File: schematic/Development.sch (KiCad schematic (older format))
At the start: 45 parts

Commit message: added partial summing difference amplifier
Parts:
- added C? (x2): C, symbol Device:C_Small
- added C? (x2): 100n, symbol Device:C_Small
- added J?: CONX, symbol Connector:Conn_Coaxial
- added J?: CONY, symbol Connector:Conn_Coaxial
- added R? (x12): R, symbol Device:R_Small
- added U? (x3): Opamp_Dual, symbol Device:Opamp_Dual_Generic
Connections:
- wire segments 158 -> 222
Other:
- note added: "PARTIAL SUMMING DIFFERENCE AMPLIFIER"

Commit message: added total summing amplifier
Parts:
- added C?: C, symbol Device:C_Small
- added J?: CONSUM, symbol Connector:Conn_Coaxial
- added R? (x5): R, symbol Device:R_Small
- added U?: OPA, Package_SO:SOIC-8_3.9x4.9mm_P1.27mm, symbol Amplifier_Operational:OPA188xxD
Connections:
- wire segments 222 -> 251
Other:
- note added: "TOTAL SUMMING AMPLIFIER"
- moved on the sheet: J?

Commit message: added test points to circuit
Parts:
- added TP? (x8): TestPoint, symbol Connector:TestPoint
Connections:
- wire segments 251 -> 267
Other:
- moved on the sheet: U?

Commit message: removed offset compensation, added bias voltage to schematic
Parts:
- removed C? (x3): Cf, symbol Device:C_Small
- removed JP? (x4): Jumper_NC_Dual, symbol Device:Jumper_NC_Dual
- removed R? (x8): R, symbol Device:R_Small
- removed R? (x3): Rf, symbol Device:R_Small
- removed RV? (x4): R_POT_TRIM, symbol Device:R_POT_TRIM
- removed TP? (x3): TestPoint, symbol Connector:TestPoint
- added C?: 330n, symbol Development-rescue:C_Small-Device
- added C?: 100n, symbol Development-rescue:C_Small-Device
- added C?: 1u, symbol Development-rescue:CP_Small-Device
- added C? (x3): 4p, symbol Development-rescue:C_Small-Device
- added R? (x3): 100k, symbol Development-rescue:R_Small-Device
- added TP? (x4): TestPoint, symbol Development-rescue:TestPoint-Connector
- added U?: L7810, symbol Regulator_Linear:L7809
- C? (x6): symbol Device:CP_Small -> Development-rescue:CP_Small-Device
- C? (x9): symbol Device:C_Small -> Development-rescue:C_Small-Device
- C?: value Cf -> 4p; symbol Device:C_Small -> Development-rescue:C_Small-Device
- D?: symbol Library:S599x -> Development-rescue:S599x-Library
- D? (x2): symbol Device:D_Schottky -> Development-rescue:D_Schottky-Device
- J?: symbol Connector:LEMO4 -> Development-rescue:LEMO4-Connector
- J? (x3): symbol Connector:Conn_Coaxial -> Development-rescue:Conn_Coaxial-Connector
- R?: value Rf -> 100k; symbol Device:R_Small -> Development-rescue:R_Small-Device
- R? (x17): symbol Device:R_Small -> Development-rescue:R_Small-Device
- TP? (x5): symbol Connector:TestPoint -> Development-rescue:TestPoint-Connector
- U? (x4): value OPA4192 -> OPA4197; symbol Device:Opamp_Quad_Generic -> Development-rescue:Opamp_Quad_Generic-Device
- U?: symbol Device:Opamp_Quad_Generic -> Development-rescue:Opamp_Quad_Generic-Device
- U?: symbol Regulator_Linear:L7812 -> Development-rescue:L7812-Regulator_Linear
- U?: symbol Regulator_Linear:L7912 -> Development-rescue:L7912-Regulator_Linear
- U? (x3): symbol Device:Opamp_Dual_Generic -> Development-rescue:Opamp_Dual_Generic-Device
- U?: symbol Amplifier_Operational:OPA188xxD -> Development-rescue:OPA188xxD-Amplifier_Operational
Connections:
- net labels added: +10V
- wire segments 267 -> 258
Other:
- note added: "BIAS VOLTAGE REGULATOR"
- note added: "SUPPLY VOLTAGE REGULATOR"
- note removed: "VOLTAGE REGULATOR"
- moved on the sheet: U?

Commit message: updated schematics
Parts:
- removed C? (x3): C, symbol Development-rescue:C_Small-Device
- removed J?: CONX, symbol Development-rescue:Conn_Coaxial-Connector
- removed J?: CONY, symbol Development-rescue:Conn_Coaxial-Connector
- removed J?: CONSUM, symbol Development-rescue:Conn_Coaxial-Connector
- removed R? (x11): R, symbol Development-rescue:R_Small-Device
- removed TP? (x4): TestPoint, symbol Development-rescue:TestPoint-Connector
- removed U?: OPA, Package_SO:SOIC-8_3.9x4.9mm_P1.27mm, symbol Development-rescue:OPA188xxD-Amplifier_Operational
- added C? (x3): 100n, symbol Development-rescue:C_Small-Device
- added R?: 100k, symbol Development-rescue:R_Small-Device
- added R? (x12): 1k, symbol Development-rescue:R_Small-Device
- added U?: OPA2917, symbol Development-rescue:Opamp_Dual_Generic-Device
- added U?: OPA2197, symbol Development-rescue:Opamp_Dual_Generic-Device
- R? (x6): value R -> 1k
- U? (x2): value Opamp_Dual -> OPA2197
- U?: value Opamp_Dual -> OPA2917
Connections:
- net labels added: -X1, -X2, -Y1, -Y2, X1+X2+Y1+Y2, X2+Y1-X1-Y2, X2+Y2-X1-Y1
- net labels removed: X1, X2, Y1, Y2
- wire segments 258 -> 248
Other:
- moved on the sheet: C?, D?, R?, U?A, U?B, U?C, U?D, U?E

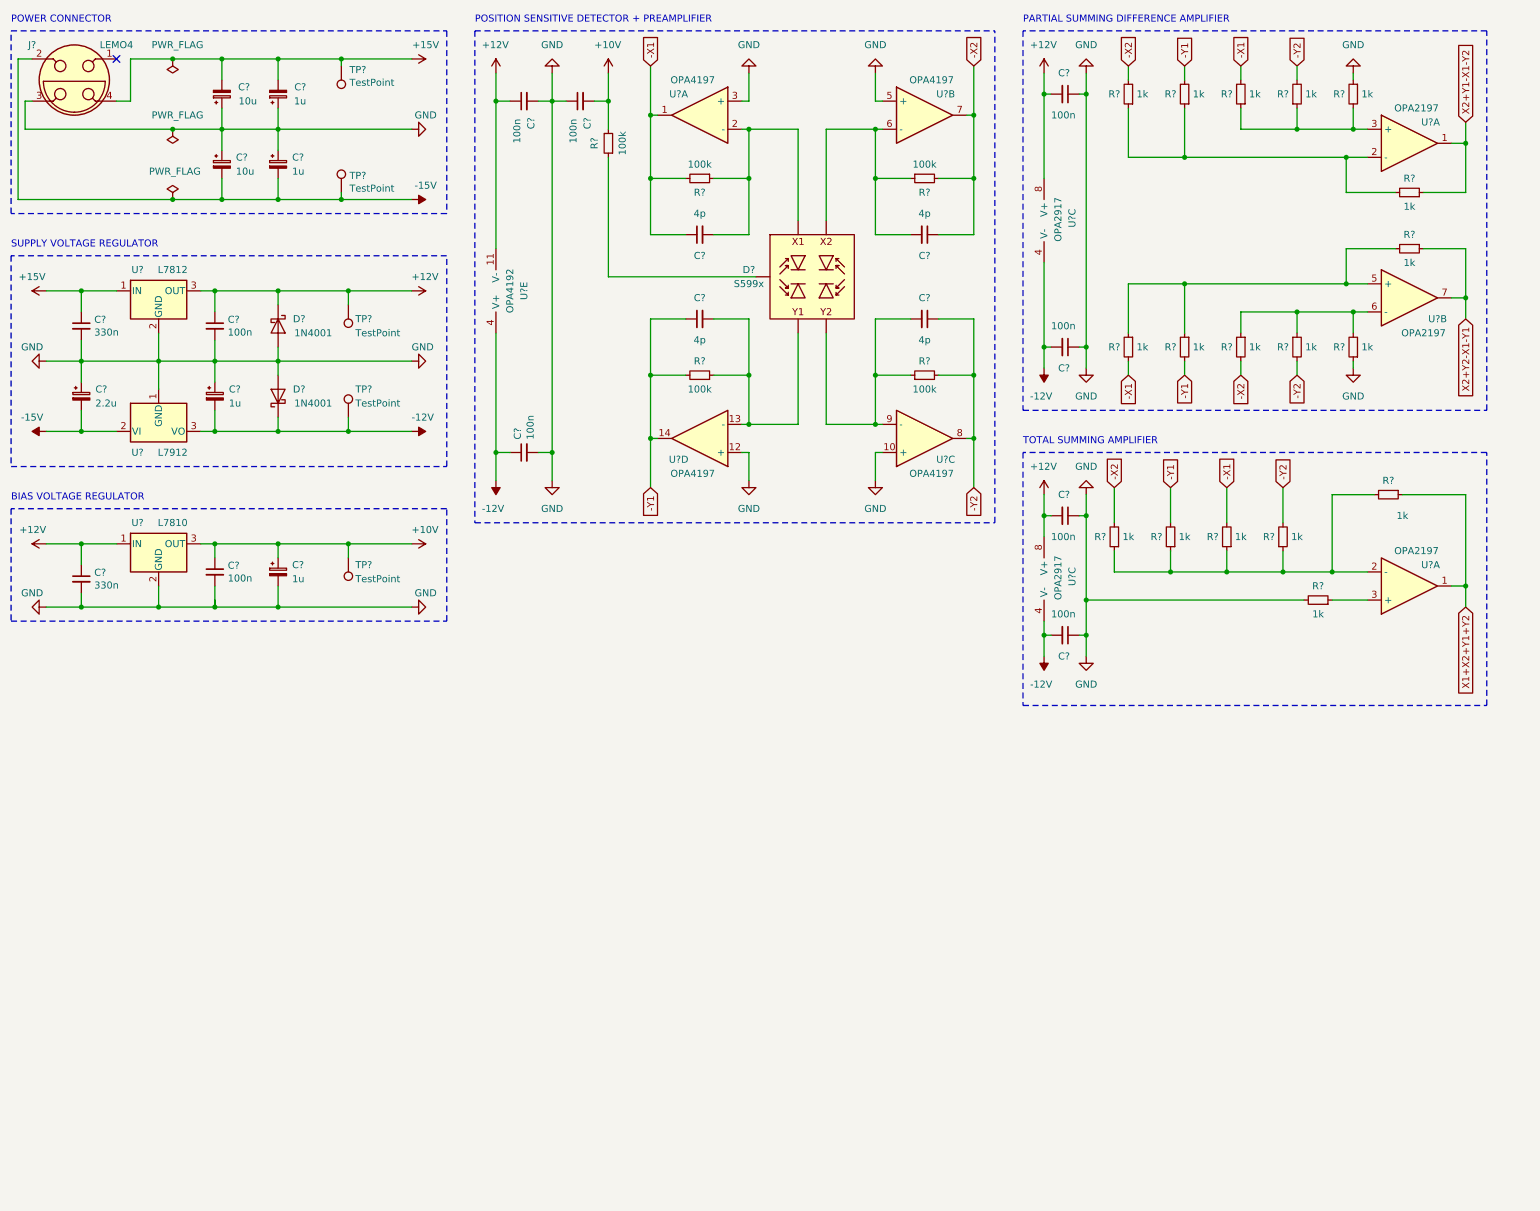
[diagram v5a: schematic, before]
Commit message: extended circuit sheet size to A3, added connectors
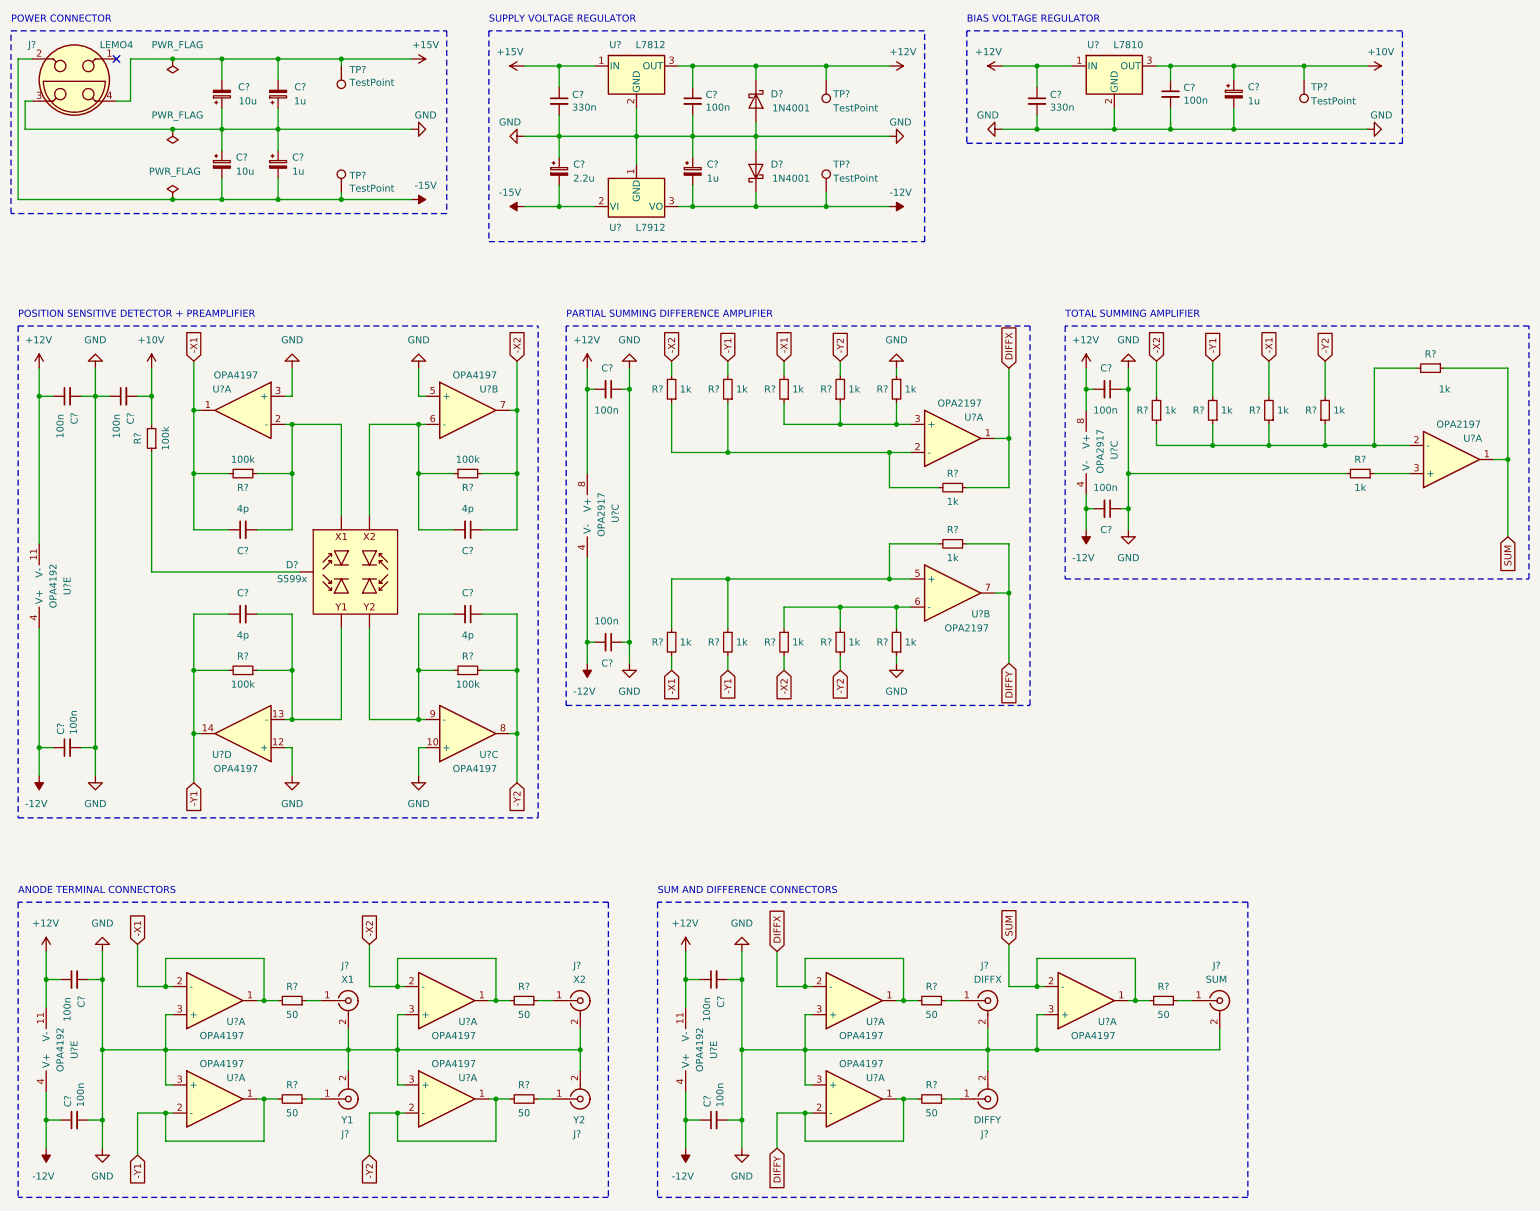
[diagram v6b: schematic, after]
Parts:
- added C? (x4): 100n, symbol Development-rescue:C_Small-Device
- added J?: X1, symbol Connector:Conn_Coaxial
- added J?: X2, symbol Connector:Conn_Coaxial
- added J?: Y1, symbol Connector:Conn_Coaxial
- added J?: Y2, symbol Connector:Conn_Coaxial
- added J?: DIFFX, symbol Connector:Conn_Coaxial
- added J?: SUM, symbol Connector:Conn_Coaxial
- added J?: DIFFY, symbol Connector:Conn_Coaxial
- added R? (x7): 50, symbol Development-rescue:R_Small-Device
- added U? (x2): OPA4192, symbol Development-rescue:Opamp_Quad_Generic-Device
- added U? (x7): OPA4197, symbol Development-rescue:Opamp_Quad_Generic-Device
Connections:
- net +12V: now also C?.1, C?.1, U?.11 (V-), U?.11 (V-)
- net -12V: now also C?.1, C?.1, U?.4 (V+), U?.4 (V+)
- net -X1: now also R?.2, U?.1, U?.2 (-)
- net -X2: now also R?.2, U?.1, U?.2 (-)
- net -Y1: now also R?.2, U?.1, U?.2 (-)
- net -Y2: now also R?.2, U?.1, U?.2 (-)
- net GND: now also C?.2, C?.2, C?.2, C?.2, J?.2 (Ext), J?.2 (Ext), J?.2 (Ext), J?.2 (Ext), J?.2 (Ext), J?.2 (Ext), J?.2 (Ext), U?.3 (+), U?.3 (+), U?.3 (+), U?.3 (+), U?.3 (+), U?.3 (+), U?.3 (+)
- net X1+X2+Y1+Y2 renamed SUM
- net SUM: now also R?.2, U?.1, U?.2 (-)
- net X2+Y1-X1-Y2 renamed DIFFX
- net DIFFX: now also R?.2, U?.1, U?.2 (-)
- net X2+Y2-X1-Y1 renamed DIFFY
- net DIFFY: now also R?.2, U?.1, U?.2 (-)
- new net: J?.1 (In), R?.1 (x7)
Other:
- note added: "ANODE TERMINAL CONNECTORS"
- note added: "SUM AND DIFFERENCE CONNECTORS"
- moved on the sheet: C?, D?, R?, TP?, U?, U?A, U?B, U?C, U?D, U?E
